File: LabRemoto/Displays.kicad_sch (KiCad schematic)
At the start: 13 parts

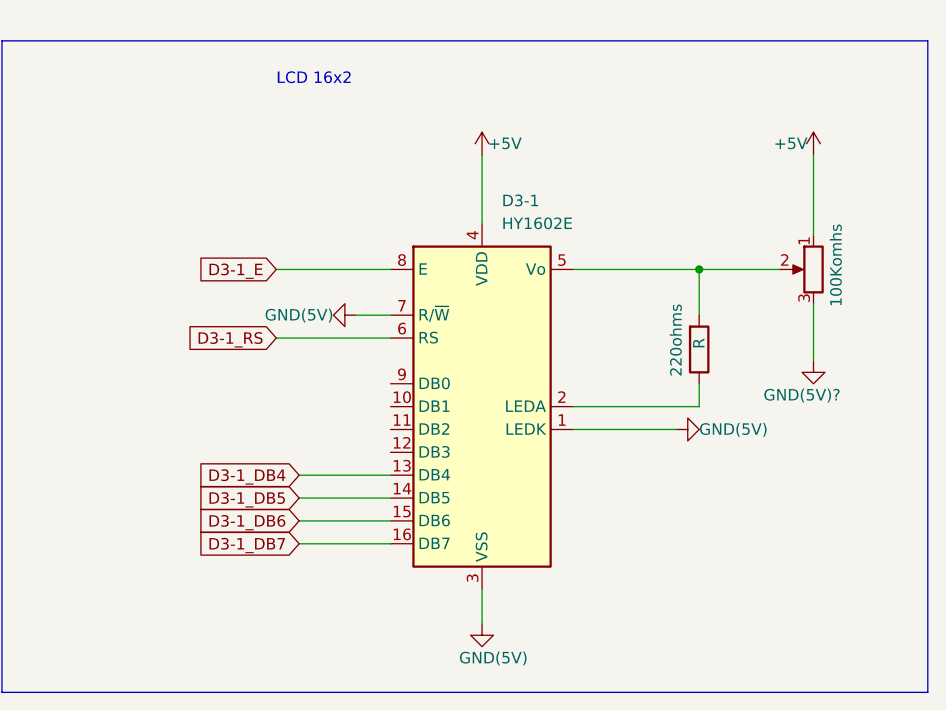
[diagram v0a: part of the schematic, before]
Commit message: Se corrigieron esquemas
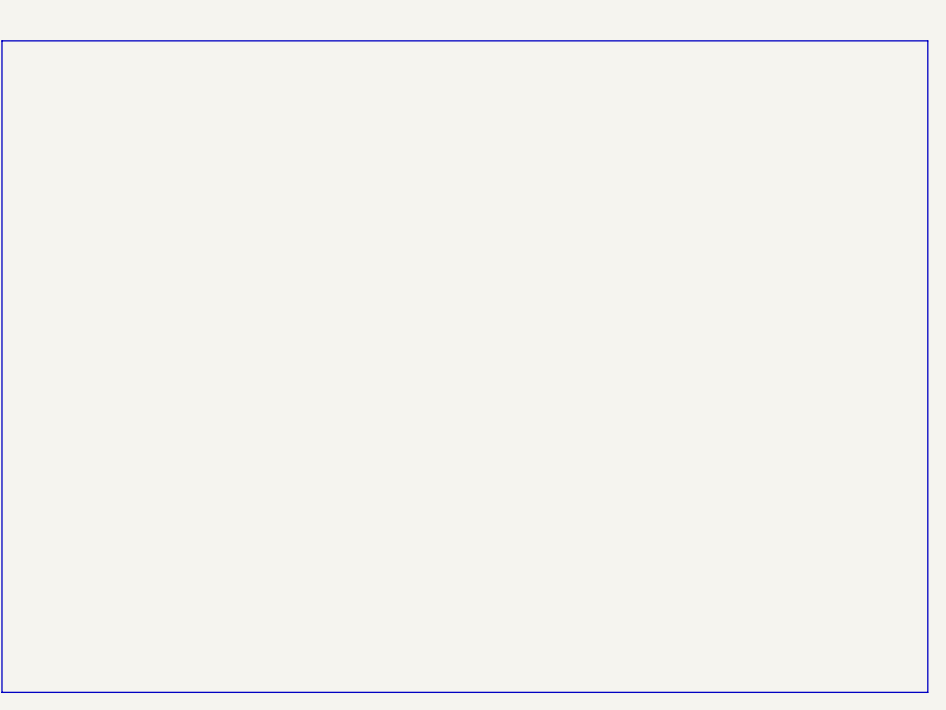
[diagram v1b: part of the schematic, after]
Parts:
- removed 100Komhs: R_Potentiometer, symbol Device:R_Potentiometer
- removed 220ohms: R, symbol Device:R
- removed D3-1: HY1602E, Display:HY1602E, symbol Display_Character:HY1602E
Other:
- note removed: "LCD 16x2"

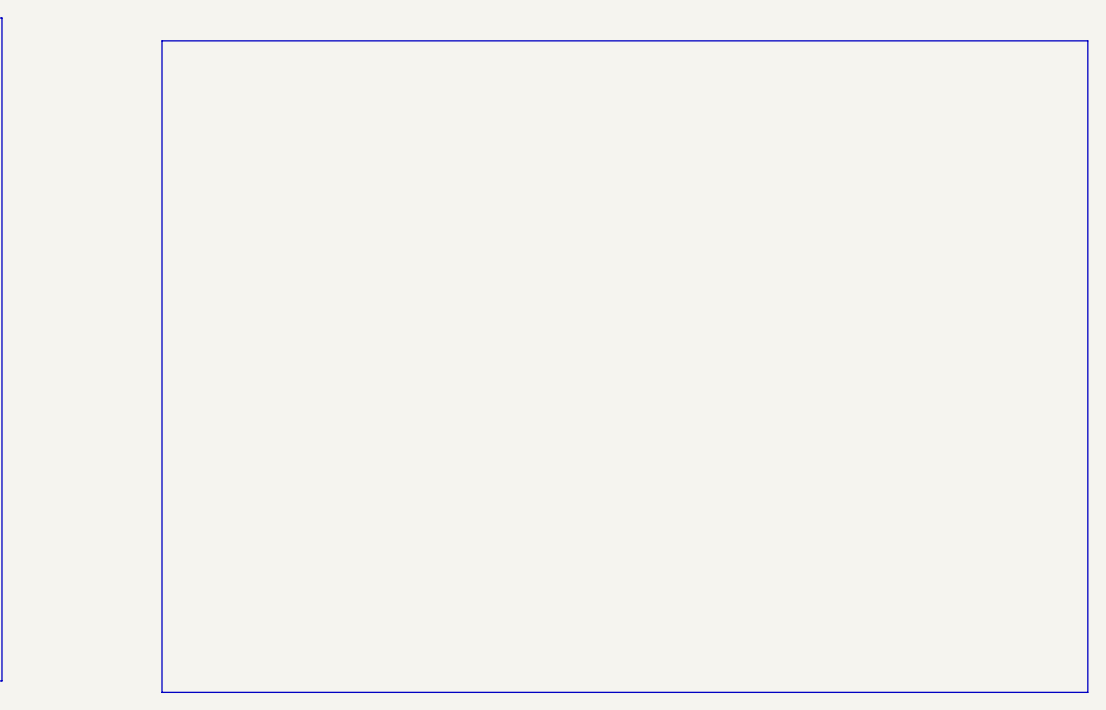
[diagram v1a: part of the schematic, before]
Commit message: Se agrego display tft
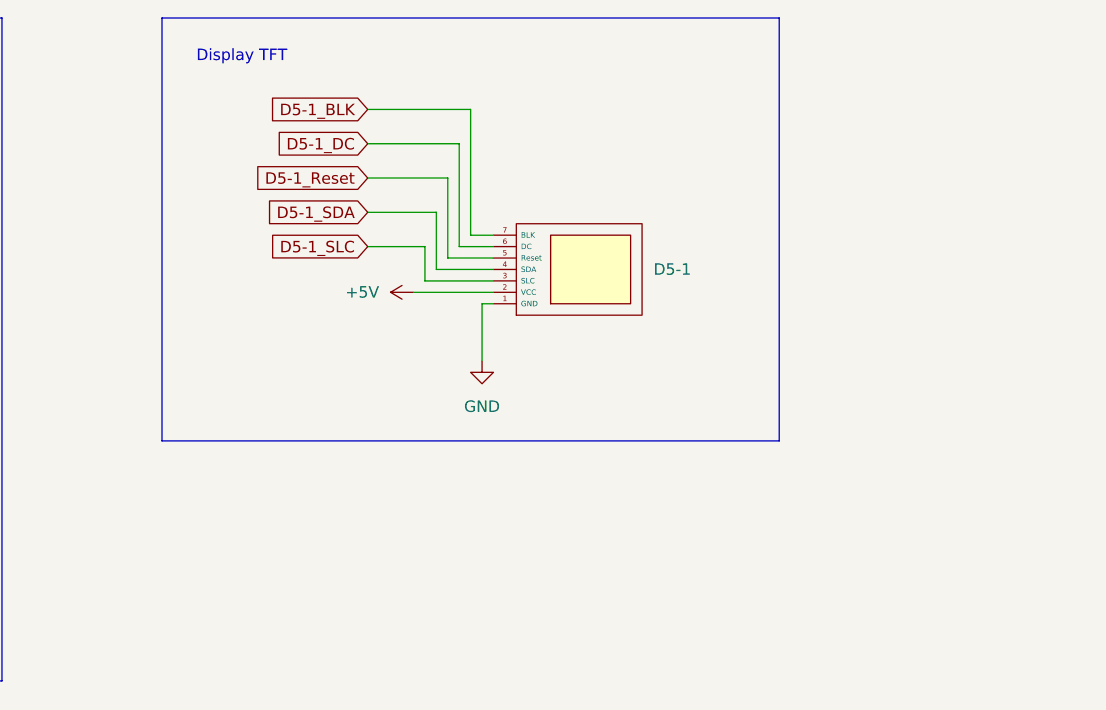
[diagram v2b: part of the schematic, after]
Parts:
- added D5-1: ~, symbol Resources:Display_TFT_
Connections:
- net +5V: now also D5-1.2 (VCC)
- net GND: now also D5-1.1 (GND)
- new net D5-1_BLK: D5-1.7 (BLK)
- new net D5-1_DC: D5-1.6 (DC)
- new net D5-1_Reset: D5-1.5 (Reset)
- new net D5-1_SDA: D5-1.4 (SDA)
- new net D5-1_SLC: D5-1.3 (SLC)
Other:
- note added: "Display TFT"
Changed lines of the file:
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@@
 (kicad_sch (version 20230121) (generator eeschema)
   (paper "A4")
-  (polyline (pts (xy 165.1 22.86) (xy 165.1 95.25))
-    (stroke (width 0) (type default))
-  )
-  (polyline (pts (xy 165.1 22.86) (xy 267.97 22.86))
+  (wire (pts (xy 198.12 45.72) (xy 201.93 45.72))
+    (stroke (width 0) (type default))
+  )
+  (wire (pts (xy 196.85 38.1) (xy 196.85 46.99))
+    (stroke (width 0) (type default))
+  )
+  (polyline (pts (xy 165.1 20.32) (xy 165.1 67.31))
+    (stroke (width 0) (type default))
+  )
+  (wire (pts (xy 198.12 34.29) (xy 198.12 45.72))
+    (stroke (width 0) (type default))
+  )
+  (polyline (pts (xy 165.1 20.32) (xy 233.68 20.32))
+    (stroke (width 0) (type default))
+  )
+  (wire (pts (xy 201.93 44.45) (xy 199.39 44.45))
+    (stroke (width 0) (type default))
+  )
+  (wire (pts (xy 199.39 44.45) (xy 199.39 30.48))
     (stroke (width 0) (type default))
   )
@@
     (stroke (width 0) (type default))
   )
+  (wire (pts (xy 187.96 41.91) (xy 195.58 41.91))
+    (stroke (width 0) (type default))
+  )
   (wire (pts (xy 124.46 55.88) (xy 127 55.88))
     (stroke (width 0) (type default))
   )
-  (polyline (pts (xy 267.97 95.25) (xy 267.97 22.86))
+  (polyline (pts (xy 233.68 67.31) (xy 233.68 20.32))
     (stroke (width 0) (type default))
   )
@@
     (stroke (width 0) (type default))
   )
-  (polyline (pts (xy 165.1 95.25) (xy 267.97 95.25))
+  (polyline (pts (xy 165.1 67.31) (xy 233.68 67.31))
+    (stroke (width 0) (type default))
+  )
+  (wire (pts (xy 199.39 30.48) (xy 187.96 30.48))
     (stroke (width 0) (type default))
   )
@@
     (stroke (width 0) (type default))
   )
+  (wire (pts (xy 196.85 46.99) (xy 201.93 46.99))
+    (stroke (width 0) (type default))
+  )
   (polyline (pts (xy 147.32 20.32) (xy 147.32 93.98))
     (stroke (width 0) (type default))
@@
     (stroke (width 0) (type default))
   )
+  (wire (pts (xy 195.58 41.91) (xy 195.58 48.26))
+    (stroke (width 0) (type default))
+  )
   (wire (pts (xy 96.52 43.18) (xy 96.52 50.8))
     (stroke (width 0) (type default))
   )
+  (wire (pts (xy 187.96 34.29) (xy 198.12 34.29))
+    (stroke (width 0) (type default))
+  )
+  (wire (pts (xy 194.31 49.53) (xy 201.93 49.53))
+    (stroke (width 0) (type default))
+  )
+  (wire (pts (xy 187.96 45.72) (xy 194.31 45.72))
+    (stroke (width 0) (type default))
+  )
+  (wire (pts (xy 193.04 50.8) (xy 201.93 50.8))
+    (stroke (width 0) (type default))
+  )
+  (wire (pts (xy 194.31 45.72) (xy 194.31 49.53))
+    (stroke (width 0) (type default))
+  )
   (polyline (pts (xy 20.32 20.32) (xy 20.32 93.98))
     (stroke (width 0) (type default))
   )
+  (wire (pts (xy 200.66 52.07) (xy 201.93 52.07))
+    (stroke (width 0) (type default))
+  )
   (wire (pts (xy 134.62 44.45) (xy 134.62 50.8))
     (stroke (width 0) (type default))
@@
   (wire (pts (xy 58.42 43.18) (xy 58.42 50.8))
     (stroke (width 0) (type default))
+  )
+  (wire (pts (xy 187.96 38.1) (xy 196.85 38.1))
+    (stroke (width 0) (type default))
+  )
+  (wire (pts (xy 200.66 58.42) (xy 200.66 52.07))
+    (stroke (width 0) (type default))
+  )
+  (wire (pts (xy 195.58 48.26) (xy 201.93 48.26))
+    (stroke (width 0) (type default))
+  )
+  (text "Display TFT\n" (at 168.91 25.4 0)
+    (effects (font (size 1.27 1.27)) (justify left bottom))
   )
   (text "4 RGBD" (at 25.4 25.4 0)
@@
     )
   )
+  (global_label "D5-1_BLK" (shape input) (at 187.96 30.48 180) (fields_autoplaced)
+    (effects (font (size 1.27 1.27)) (justify right))
+    (property "Intersheetrefs" "${INTERSHEET_REFS}" (at 175.1777 30.48 0)
+      (effects (font (size 1.27 1.27)) (justify right) hide)
+    )
+  )
+  (global_label "D5-1_Reset" (shape input) (at 187.96 38.1 180) (fields_autoplaced)
+    (effects (font (size 1.27 1.27)) (justify right))
+    (property "Intersheetrefs" "${INTERSHEET_REFS}" (at 173.5448 38.1 0)
+      (effects (font (size 1.27 1.27)) (justify right) hide)
+    )
+  )
   (global_label "D4-1_INR" (shape input) (at 38.1 55.88 180) (fields_autoplaced)
     (effects (font (size 1.27 1.27)) (justify right))
     (property "Intersheetrefs" "${INTERSHEET_REFS}" (at 25.6805 55.88 0)
+      (effects (font (size 1.27 1.27)) (justify right) hide)
+    )
+  )
+  (global_label "D5-1_SLC" (shape input) (at 187.96 45.72 180) (fields_autoplaced)
+    (effects (font (size 1.27 1.27)) (justify right))
+    (property "Intersheetrefs" "${INTERSHEET_REFS}" (at 175.2382 45.72 0)
+      (effects (font (size 1.27 1.27)) (justify right) hide)
+    )
+  )
+  (global_label "D5-1_SDA" (shape input) (at 187.96 41.91 180) (fields_autoplaced)
+    (effects (font (size 1.27 1.27)) (justify right))
+    (property "Intersheetrefs" "${INTERSHEET_REFS}" (at 175.1777 41.91 0)
+      (effects (font (size 1.27 1.27)) (justify right) hide)
+    )
+  )
+  (global_label "D5-1_DC" (shape input) (at 187.96 34.29 180) (fields_autoplaced)
+    (effects (font (size 1.27 1.27)) (justify right))
+    (property "Intersheetrefs" "${INTERSHEET_REFS}" (at 176.2058 34.29 0)
       (effects (font (size 1.27 1.27)) (justify right) hide)
     )
@@
     )
   )
+  (symbol (lib_id "Resources:Display_TFT_") (at 210.82 48.26 0) (mirror x) (unit 1)
+    (in_bom yes) (on_board yes) (dnp no)
+    (property "Reference" "D5-1" (at 219.71 48.26 0)
+      (effects (font (size 1.27 1.27)) (justify left))
+    )
+    (property "Value" "~" (at 208.28 50.8 0)
+      (effects (font (size 1.27 1.27)))
+    )
+    (property "Footprint" "" (at 208.28 50.8 0)
+      (effects (font (size 1.27 1.27)) hide)
+    )
+    (property "Datasheet" "" (at 208.28 50.8 0)
+      (effects (font (size 1.27 1.27)) hide)
+    )
+    (pin "6")
+    (pin "7")
+    (pin "2")
+    (pin "3")
+    (pin "1")
+    (pin "5")
+    (pin "4")
+    (instances
+      (project "Displays"
+        (path "/b0802cdf-af6e-4f0c-bb3c-0f54413071d6"
+          (reference "D5-1") (unit 1)
+        )
+      )
+    )
+  )
   (symbol (lib_id "Device:R") (at 44.45 55.88 270) (unit 1)
     (in_bom yes) (on_board yes) (dnp no)
@@
         (path "/b0802cdf-af6e-4f0c-bb3c-0f54413071d6"
           (reference "#PWR?") (unit 1)
+        )
+      )
+    )
+  )
+  (symbol (lib_name "+5V_1") (lib_id "power:+5V") (at 193.04 50.8 90) (unit 1)
+    (in_bom yes) (on_board yes) (dnp no) (fields_autoplaced)
+    (property "Reference" "#PWR01" (at 196.85 50.8 0)
+      (effects (font (size 1.27 1.27)) hide)
+    )
+    (property "Value" "+5V" (at 189.23 50.8 90)
+      (effects (font (size 1.27 1.27)) (justify left))
+    )
+    (property "Footprint" "" (at 193.04 50.8 0)
+      (effects (font (size 1.27 1.27)) hide)
+    )
+    (property "Datasheet" "" (at 193.04 50.8 0)
+      (effects (font (size 1.27 1.27)) hide)
+    )
+    (pin "1")
+    (instances
+      (project "Displays"
+        (path "/b0802cdf-af6e-4f0c-bb3c-0f54413071d6"
+          (reference "#PWR01") (unit 1)
         )
       )
@@
         )
       )
+    )
+  )
+  (symbol (lib_name "GND_1") (lib_id "power:GND") (at 200.66 58.42 0) (unit 1)
+    (in_bom yes) (on_board yes) (dnp no) (fields_autoplaced)
+    (property "Reference" "#PWR02" (at 200.66 64.77 0)
+      (effects (font (size 1.27 1.27)) hide)
+    )
+    (property "Value" "GND" (at 200.66 63.5 0)
+      (effects (font (size 1.27 1.27)))
+    )
+    (property "Footprint" "" (at 200.66 58.42 0)
+      (effects (font (size 1.27 1.27)) hide)
+    )
+    (property "Datasheet" "" (at 200.66 58.42 0)
+      (effects (font (size 1.27 1.27)) hide)
+    )
+    (pin "1")
+    (instances
+      (project "Displays"
+        (path "/b0802cdf-af6e-4f0c-bb3c-0f54413071d6"
+          (reference "#PWR02") (unit 1)
+        )
+      )

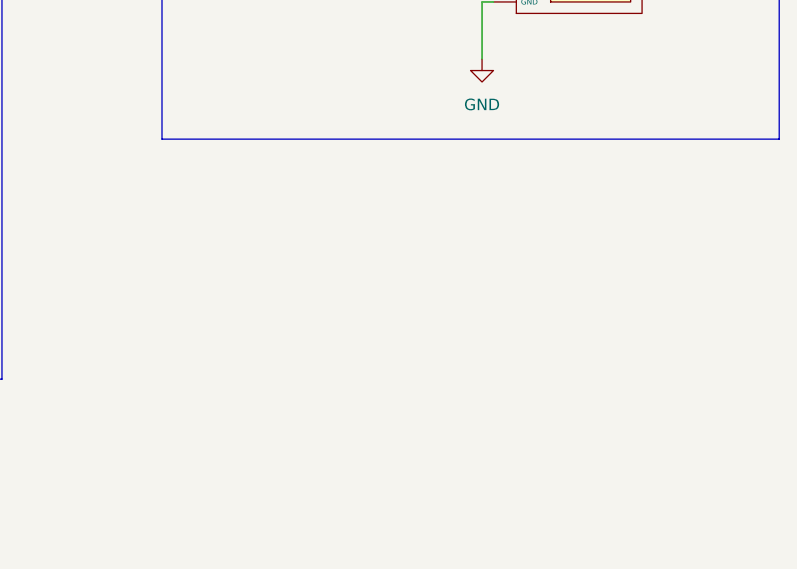
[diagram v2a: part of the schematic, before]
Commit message: Sa añadio HC-SR04
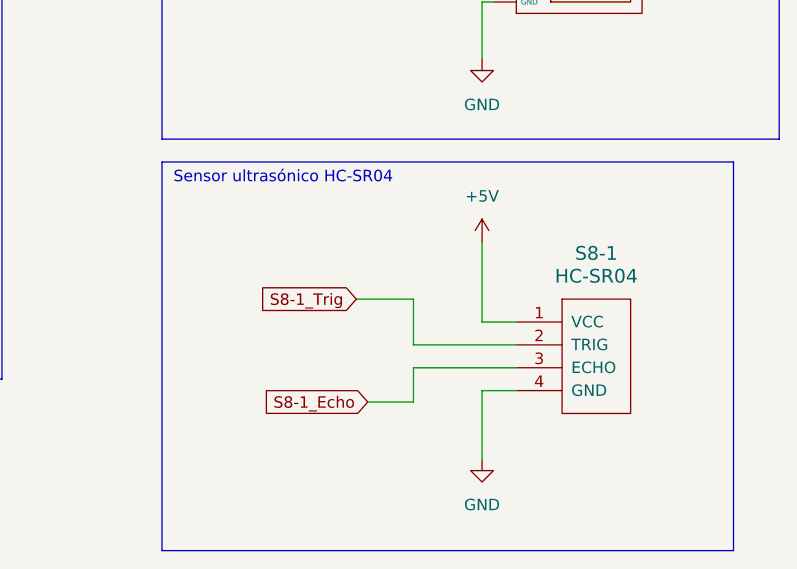
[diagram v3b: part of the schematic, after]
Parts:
- added S8-1: HC-SR04, symbol hc-sr04:HC-SR04
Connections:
- net +5V: now also S8-1.1 (VCC)
- net GND: now also S8-1.4 (GND)
- new net S8-1_Echo: S8-1.3 (ECHO)
- new net S8-1_Trig: S8-1.2 (TRIG)
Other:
- note added: "Sensor ultrasónico HC-SR04"
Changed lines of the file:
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@@
+    (stroke (width 0) (type default))
+  )
+  (wire (pts (xy 193.04 96.52) (xy 193.04 92.71))
     (stroke (width 0) (type default))
   )
@@
     (stroke (width 0) (type default))
   )
+  (wire (pts (xy 193.04 90.17) (xy 204.47 90.17))
+    (stroke (width 0) (type default))
+  )
   (wire (pts (xy 87.63 55.88) (xy 88.9 55.88))
     (stroke (width 0) (type default))
@@
     (stroke (width 0) (type default))
   )
+  (wire (pts (xy 187.96 96.52) (xy 193.04 96.52))
+    (stroke (width 0) (type default))
+  )
   (wire (pts (xy 195.58 41.91) (xy 195.58 48.26))
     (stroke (width 0) (type default))
@@
     (stroke (width 0) (type default))
   )
+  (wire (pts (xy 193.04 92.71) (xy 204.47 92.71))
+    (stroke (width 0) (type default))
+  )
+  (wire (pts (xy 200.66 102.87) (xy 200.66 95.25))
+    (stroke (width 0) (type default))
+  )
   (wire (pts (xy 187.96 45.72) (xy 194.31 45.72))
     (stroke (width 0) (type default))
@@
     (stroke (width 0) (type default))
   )
+  (wire (pts (xy 200.66 95.25) (xy 204.47 95.25))
+    (stroke (width 0) (type default))
+  )
   (wire (pts (xy 134.62 44.45) (xy 134.62 50.8))
     (stroke (width 0) (type default))
@@
     (stroke (width 0) (type default))
   )
+  (wire (pts (xy 200.66 78.74) (xy 200.66 87.63))
+    (stroke (width 0) (type default))
+  )
+  (wire (pts (xy 200.66 87.63) (xy 204.47 87.63))
+    (stroke (width 0) (type default))
+  )
   (wire (pts (xy 58.42 68.58) (xy 58.42 60.96))
     (stroke (width 0) (type default))
   )
+  (wire (pts (xy 186.69 85.09) (xy 193.04 85.09))
+    (stroke (width 0) (type default))
+  )
+  (wire (pts (xy 193.04 85.09) (xy 193.04 90.17))
+    (stroke (width 0) (type default))
+  )
   (wire (pts (xy 101.6 68.58) (xy 134.62 68.58))
     (stroke (width 0) (type default))
@@
   (wire (pts (xy 195.58 48.26) (xy 201.93 48.26))
     (stroke (width 0) (type default))
+  )
+  (rectangle (start 165.1 69.85) (end 228.6 113.03)
+    (stroke (width 0) (type default))
+    (fill (type none))
   )
   (text "Display TFT\n" (at 168.91 25.4 0)
@@
     (effects (font (size 1.27 1.27)) (justify left bottom))
   )
+  (text "Sensor ultrasónico HC-SR04\n" (at 166.37 72.39 0)
+    (effects (font (size 1.27 1.27)) (justify left bottom))
+  )
   (global_label "D4-1_B" (shape input) (at 114.3 55.88 180) (fields_autoplaced)
     (effects (font (size 1.27 1.27)) (justify right))
@@
     )
   )
+  (global_label "S8-1_Echo" (shape input) (at 187.96 96.52 180) (fields_autoplaced)
+    (effects (font (size 1.27 1.27)) (justify right))
+    (property "Intersheetrefs" "${INTERSHEET_REFS}" (at 174.2707 96.52 0)
+      (effects (font (size 1.27 1.27)) (justify right) hide)
+    )
+  )
   (global_label "D5-1_BLK" (shape input) (at 187.96 30.48 180) (fields_autoplaced)
     (effects (font (size 1.27 1.27)) (justify right))
@@
     )
   )
+  (global_label "S8-1_Trig" (shape input) (at 186.69 85.09 180) (fields_autoplaced)
+    (effects (font (size 1.27 1.27)) (justify right))
+    (property "Intersheetrefs" "${INTERSHEET_REFS}" (at 174.0287 85.09 0)
+      (effects (font (size 1.27 1.27)) (justify right) hide)
+    )
+  )
   (global_label "D5-1_Reset" (shape input) (at 187.96 38.1 180) (fields_autoplaced)
     (effects (font (size 1.27 1.27)) (justify right))
@@
         (path "/b0802cdf-af6e-4f0c-bb3c-0f54413071d6"
           (reference "GND(5V)") (unit 1)
+        )
+      )
+    )
+  )
+  (symbol (lib_id "hc-sr04:HC-SR04") (at 209.55 91.44 0) (mirror y) (unit 1)
+    (in_bom yes) (on_board yes) (dnp no)
+    (property "Reference" "S8-1" (at 213.36 80.01 0)
+      (effects (font (size 1.524 1.524)))
+    )
+    (property "Value" "HC-SR04" (at 213.36 82.55 0)
+      (effects (font (size 1.524 1.524)))
+    )
+    (property "Footprint" "" (at 209.55 91.44 0)
+      (effects (font (size 1.524 1.524)))
+    )
+    (property "Datasheet" "" (at 209.55 91.44 0)
+      (effects (font (size 1.524 1.524)))
+    )
+    (pin "3")
+    (pin "4")
+    (pin "2")
+    (pin "1")
+    (instances
+      (project "Displays"
+        (path "/b0802cdf-af6e-4f0c-bb3c-0f54413071d6"
+          (reference "S8-1") (unit 1)
         )
       )
@@
     )
   )
+  (symbol (lib_name "+5V_2") (lib_id "power:+5V") (at 200.66 78.74 0) (unit 1)
+    (in_bom yes) (on_board yes) (dnp no) (fields_autoplaced)
+    (property "Reference" "#PWR03" (at 200.66 82.55 0)
+      (effects (font (size 1.27 1.27)) hide)
+    )
+    (property "Value" "+5V" (at 200.66 73.66 0)
+      (effects (font (size 1.27 1.27)))
+    )
+    (property "Footprint" "" (at 200.66 78.74 0)
+      (effects (font (size 1.27 1.27)) hide)
+    )
+    (property "Datasheet" "" (at 200.66 78.74 0)
+      (effects (font (size 1.27 1.27)) hide)
+    )
+    (pin "1")
+    (instances
+      (project "Displays"
+        (path "/b0802cdf-af6e-4f0c-bb3c-0f54413071d6"
+          (reference "#PWR03") (unit 1)
+        )
+      )
+    )
+  )
   (symbol (lib_id "Device:R") (at 44.45 55.88 270) (unit 1)
     (in_bom yes) (on_board yes) (dnp no)
@@
         )
       )
+    )
+  )
+  (symbol (lib_name "GND_2") (lib_id "power:GND") (at 200.66 102.87 0) (unit 1)
+    (in_bom yes) (on_board yes) (dnp no) (fields_autoplaced)
+    (property "Reference" "#PWR04" (at 200.66 109.22 0)
+      (effects (font (size 1.27 1.27)) hide)
+    )
+    (property "Value" "GND" (at 200.66 107.95 0)
+      (effects (font (size 1.27 1.27)))
+    )
+    (property "Footprint" "" (at 200.66 102.87 0)
+      (effects (font (size 1.27 1.27)) hide)
+    )
+    (property "Datasheet" "" (at 200.66 102.87 0)
+      (effects (font (size 1.27 1.27)) hide)
+    )
+    (pin "1")
+    (instances
+      (project "Displays"
+        (path "/b0802cdf-af6e-4f0c-bb3c-0f54413071d6"
+          (reference "#PWR04") (unit 1)
+        )
+      )
